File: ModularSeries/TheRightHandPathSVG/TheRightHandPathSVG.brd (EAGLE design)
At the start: 76 x 83 mm, 79 parts, among them IC1 ATTINY861, IC2 SN74HCX38, IC3 SN74HCX38

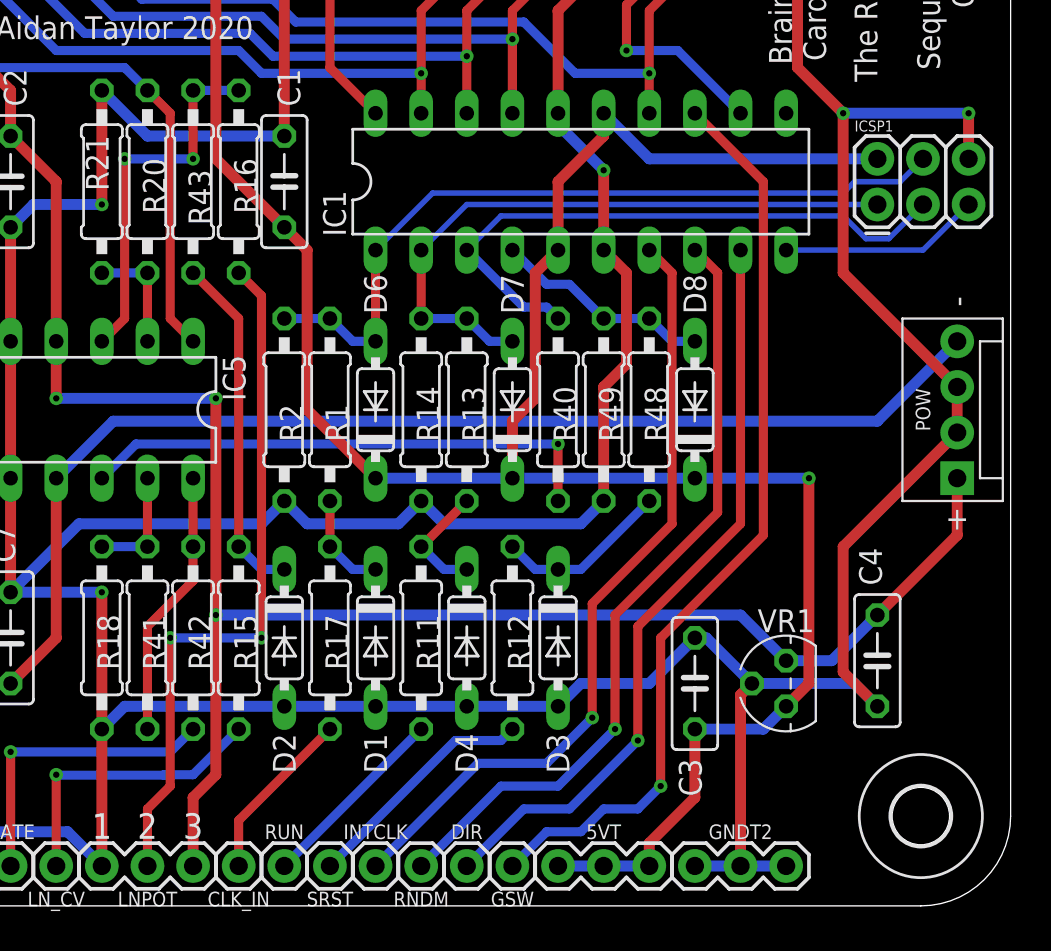
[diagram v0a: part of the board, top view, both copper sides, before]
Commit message: Power header updated on most PCBs. Knives layout added
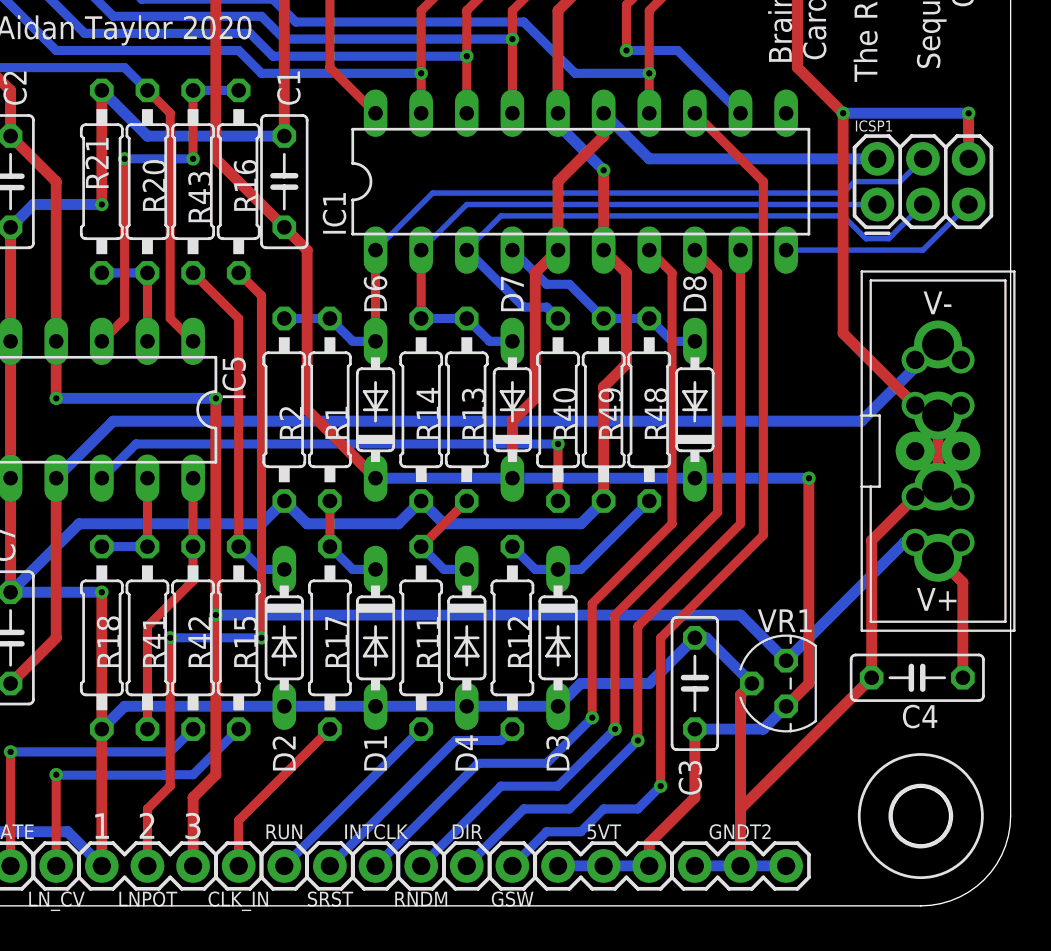
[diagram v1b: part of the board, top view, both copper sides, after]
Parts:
- removed POW: 4XMOLEX, ElectricNoodleBox:MOLEX-1X4
- added WP1: COMBO_SUPPLY_HEADER, ElectricNoodleBox:COMBINED_POWER
- moved C4 2.42 mm to (70.8, 12.7), turned to 180 degrees
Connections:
- net +12V: now also WP1.V+1, WP1.V+2, WP1.V+3; no longer POW.1
- net -12V: now also WP1.V-1, WP1.V-2, WP1.V-3; no longer POW.4
- net AGND: now also WP1.GND1, WP1.GND2, WP1.GND3, WP1.GND4, WP1.GND5, WP1.GND6, WP1.GND7, WP1.GND8; no longer POW.2, POW.3
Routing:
- net AGND: track 386.0 -> 391.2 mm
- net +12V: track 190.0 -> 194.8 mm
- net -12V: track 65.8 -> 67.9 mm
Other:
- board text removed: "+"
- board text removed: "-"

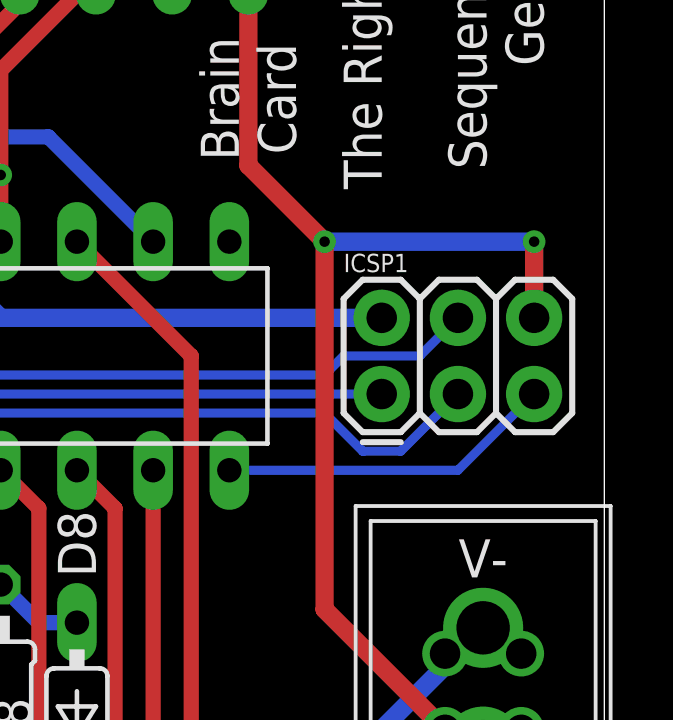
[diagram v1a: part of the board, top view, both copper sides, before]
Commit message: BOM, panel wiring and documentation complete for TimeSeed
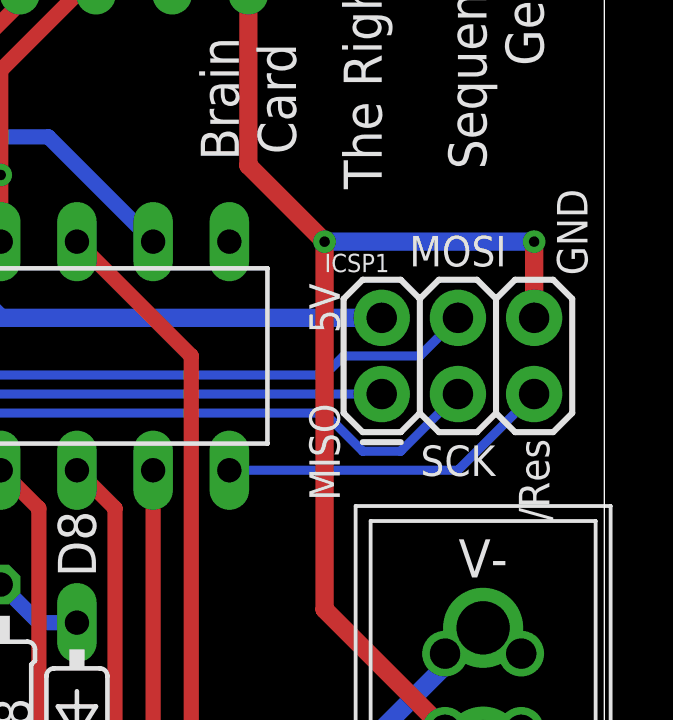
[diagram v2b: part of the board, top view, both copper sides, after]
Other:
- board text added: "/Res"
- board text added: "5V"
- board text added: "GND"
- board text added: "MISO"
- board text added: "MOSI"
- board text added: "SCK"
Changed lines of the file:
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@@
 <dimension x1="5" y1="5" x2="71" y2="5" x3="38" y3="-2" textsize="1.27" textratio="16" layer="21"/>
 <dimension x1="0" y1="0" x2="76" y2="0" x3="38" y3="-4" textsize="1.27" textratio="16" layer="21"/>
+<text x="66.675" y="38.735" size="1.016" layer="21" font="vector" rot="R270" align="center-left">MISO</text>
+<text x="71.12" y="36.83" size="1.016" layer="21" font="vector" align="center">SCK</text>
+<text x="73.66" y="36.195" size="1.016" layer="21" font="vector" rot="R90" align="center">/Res</text>
+<text x="66.675" y="41.91" size="1.016" layer="21" font="vector" rot="R90" align="center">5V</text>
+<text x="71.12" y="43.815" size="1.016" layer="21" font="vector" rot="R180" align="center">MOSI</text>
+<text x="74.93" y="44.45" size="1.016" layer="21" font="vector" rot="R90" align="center">GND</text>
 </plain>
 <attributes>
@@
 </element>
 <element name="ICSP1" library="ElectricNoodleBox" package="2X3" value="ICSP_2.54" x="68.58" y="39.0525" smashed="yes">
-<attribute name="NAME" x="67.31" y="43.1165" size="0.6096" layer="25" font="vector" ratio="20"/>
+<attribute name="NAME" x="66.675" y="43.1165" size="0.6096" layer="25" font="vector" ratio="20"/>
 <attribute name="VALUE" x="67.31" y="36.6395" size="0.6096" layer="27" font="vector" ratio="20"/>
 </element>

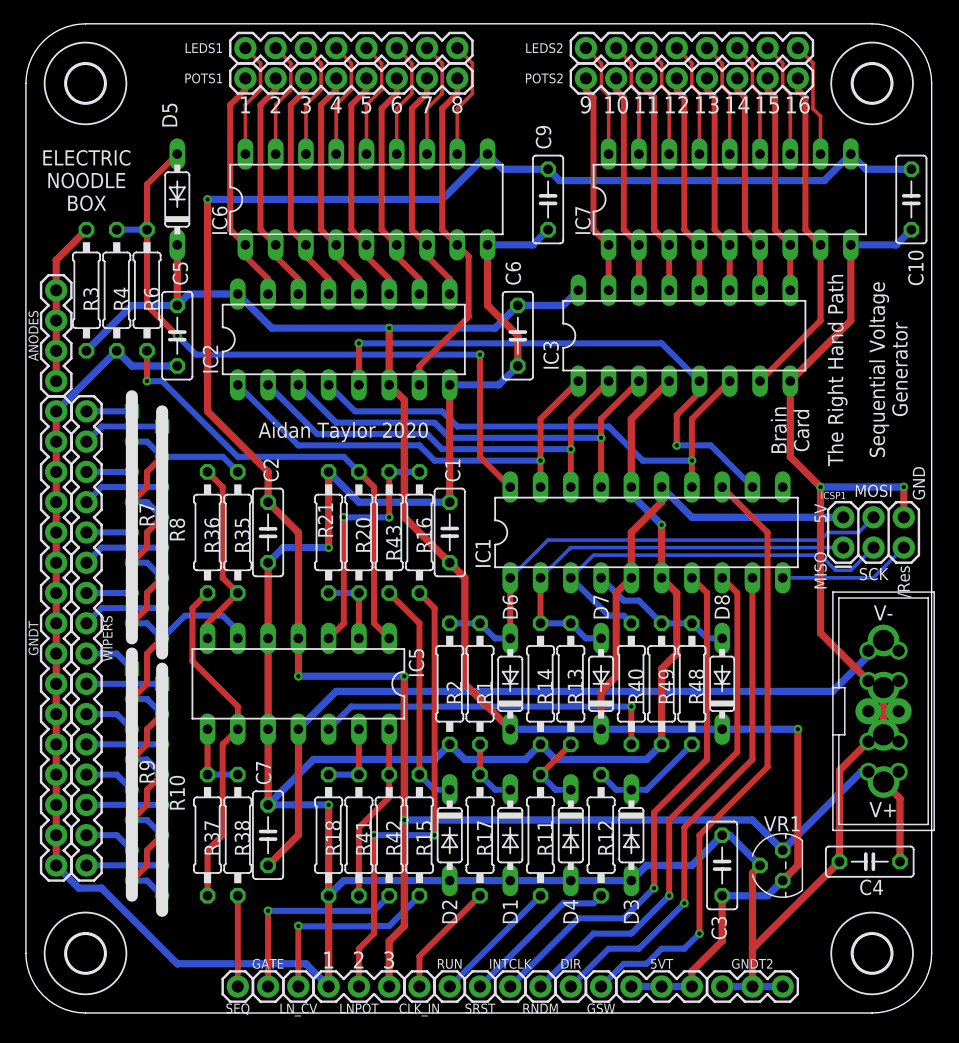
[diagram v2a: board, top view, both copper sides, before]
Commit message: TRHP-SVG version 2, Endings added and Mirrors updated
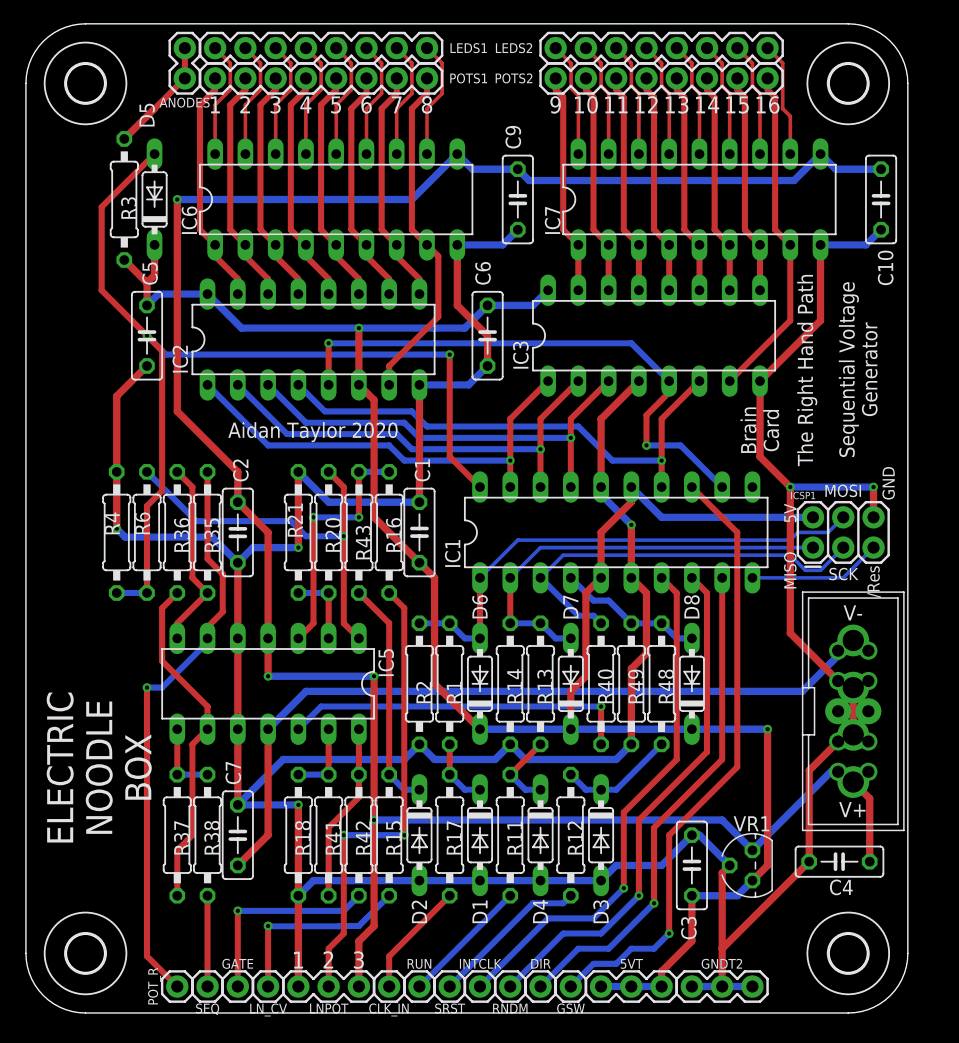
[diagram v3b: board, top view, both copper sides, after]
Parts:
- removed GNDT, WIPERS: (no value), ElectricNoodleBox:1X16
- removed R10, R7, R8, R9: 10K, ElectricNoodleBox:4_ISO_RES_NET_2.54
- added POT_R: 1XWIREPAD, ElectricNoodleBox:1X01
- ANODES: value 4XWIREPAD -> 2XWIREPAD; device ElectricNoodleBox:1X04 -> ElectricNoodleBox:1X02
- moved ANODES 27.6 mm to (13.3, 78.4)
- moved R4 20.3 mm to (7.62, 40.3), turned to 90 degrees
- moved R6 20.3 mm to (10.2, 40.3), turned to 90 degrees
- moved R3 8.26 mm to (8.26, 68.3)
- moved C10 2.54 mm to (71.8, 68.3)
- moved R49 2.54 mm to (50.8, 27.6)
- moved CLK_IN 2.54 mm to (30.5, 2.22)
- moved IC2 2.54 mm to (24.1, 56.5)
- moved R15 2.54 mm to (30.5, 14.9)
- moved R16 2.54 mm to (30.5, 40.3)
- moved R20 2.54 mm to (25.4, 40.3)
- moved R41 2.54 mm to (25.4, 14.9)
- moved R35 2.54 mm to (15.2, 40.3)
- moved R36 2.54 mm to (12.7, 40.3)
- moved R37 2.54 mm to (12.7, 14.9)
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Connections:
- removed net N$31: R7.P$3, WIPERS.3
- removed net N$33: R7.P$5, WIPERS.5
- removed net N$35: R7.P$7, WIPERS.7
- removed net N$37: R9.P$5, WIPERS.13
- removed net N$39: R10.P$5, WIPERS.14
- removed net N$41: R9.P$7, WIPERS.15
- removed net N$42: R7.P$1, WIPERS.1
- removed net N$43: R8.P$1, WIPERS.2
- removed net N$45: R8.P$3, WIPERS.4
- removed net N$47: R8.P$5, WIPERS.6
- removed net N$49: R8.P$7, WIPERS.8
- removed net N$50: R9.P$1, WIPERS.9
- removed net N$51: R10.P$1, WIPERS.10
- removed net N$52: R9.P$3, WIPERS.11
- removed net N$53: R10.P$3, WIPERS.12
- removed net N$57: R10.P$7, WIPERS.16
- removed net N$58: IC5.6, R10.P$2, R10.P$4, R10.P$6, R10.P$8, R35.2, R7.P$2, R7.P$4, R7.P$6, R7.P$8, R8.P$2, R8.P$4, R8.P$6, R8.P$8, R9.P$2, R9.P$4, R9.P$6, R9.P$8
- new net N$48: IC5.6, POT_R.1, R35.2
- net AGND: no longer GNDT.1, GNDT.10, GNDT.11, GNDT.12, GNDT.13, GNDT.14, GNDT.15, GNDT.16, GNDT.2, GNDT.3, GNDT.4, GNDT.5, GNDT.6, GNDT.7, GNDT.8, GNDT.9
- net N$7: no longer ANODES.3, ANODES.4
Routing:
- net N$58: track 75.0 -> 0.00 mm
- net AGND: track 391.2 -> 339.3 mm, vias 5 -> 6
- net N$48: track 0.00 -> 48.1 mm, vias 0 -> 1
- net N$17: track 58.1 -> 82.1 mm
- net N$47: track 6.88 -> 0.00 mm
- net N$45: track 6.88 -> 0.00 mm
- net N$49: track 6.88 -> 0.00 mm
- net N$43: track 6.88 -> 0.00 mm
- net N$57: track 6.35 -> 0.00 mm
- net N$53: track 6.35 -> 0.00 mm
- net N$51: track 6.35 -> 0.00 mm
- net N$39: track 6.35 -> 0.00 mm
- net +5V: track 184.1 -> 177.9 mm
- net N$15: track 38.5 -> 33.8 mm
- net N$50: track 4.34 -> 0.00 mm
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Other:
- board size 76 x 83 mm -> 74 x 83 mm
